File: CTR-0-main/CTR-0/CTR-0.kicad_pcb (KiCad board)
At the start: 2 copper layers, 21 x 51 mm, 35 parts, among them J1 USB_C_Receptacle_USB2.0_14P, J2 Conn_01x20, J3 Conn_01x20, J4 Conn_01x03, SW1 SW_Push, U1 RP2040, U2 NCP1117-3.3_SOT223, U3 W25Q128JVS, U4 TVS1400DRV, Y1 12MHz

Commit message: final first route
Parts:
- C10, C11, C12, C13, C14, C15, C16, C6, C7, C8, C9: moved to B.Cu
- moved C8 59.9 mm to (193.5, 103.2)
- moved C7 59.5 mm to (193.5, 100.5)
- moved C10 58.4 mm to (195.0, 97.0), turned to 0 degrees
- moved C12 57.7 mm to (192.2, 105.0)
- moved C9 57.7 mm to (192.0, 99.5), turned to -90 degrees
- moved C13 55.6 mm to (191.8, 103.2), turned to 90 degrees
- moved C11 55.2 mm to (189.2, 103.2), turned to 90 degrees
- moved C6 55.2 mm to (188.8, 98.5), turned to 90 degrees
- moved C16 52.5 mm to (190.0, 101.5), turned to 0 degrees
- moved C14 52.0 mm to (194.8, 83.7), turned to -90 degrees
- moved C15 51.8 mm to (188.0, 101.5)
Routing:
- net +1V1: track 16.2 -> 17.5 mm, vias 0 -> 2

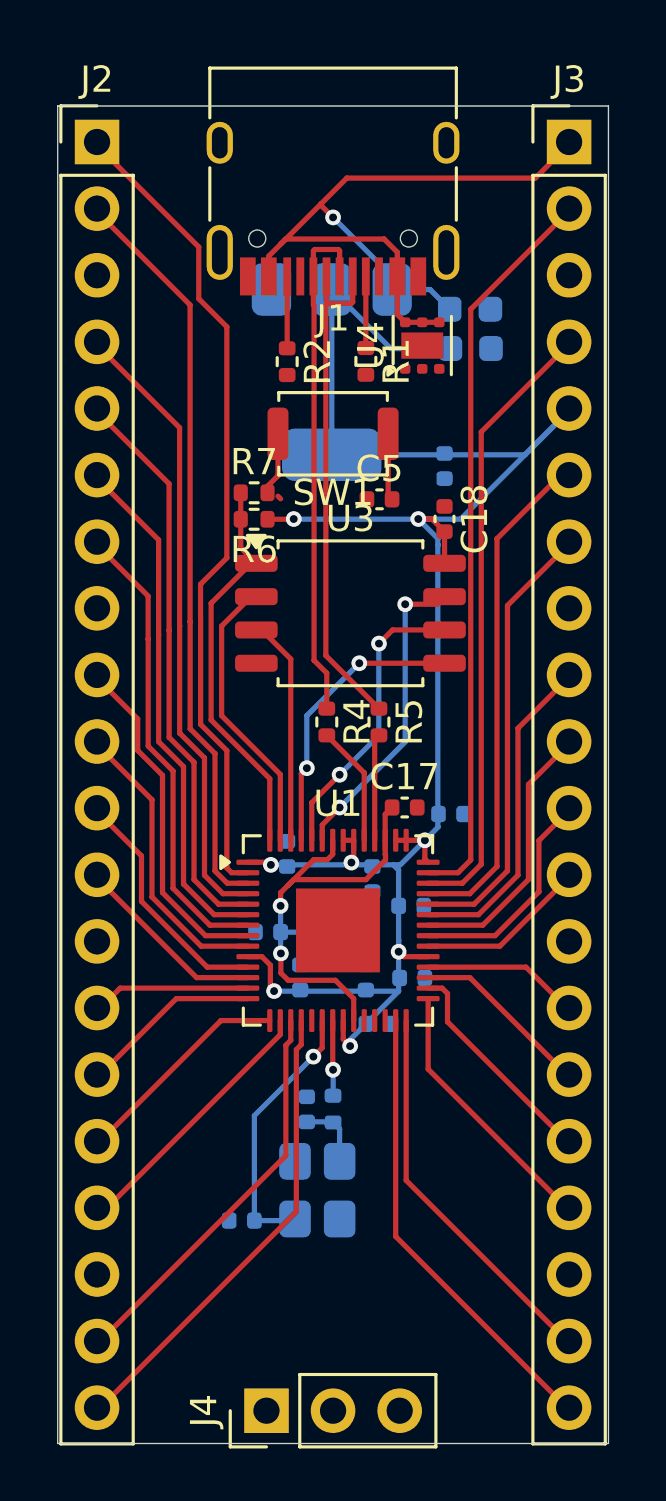
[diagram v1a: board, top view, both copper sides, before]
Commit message: reroute #2
does not fulfill drc, fix errors and clearance
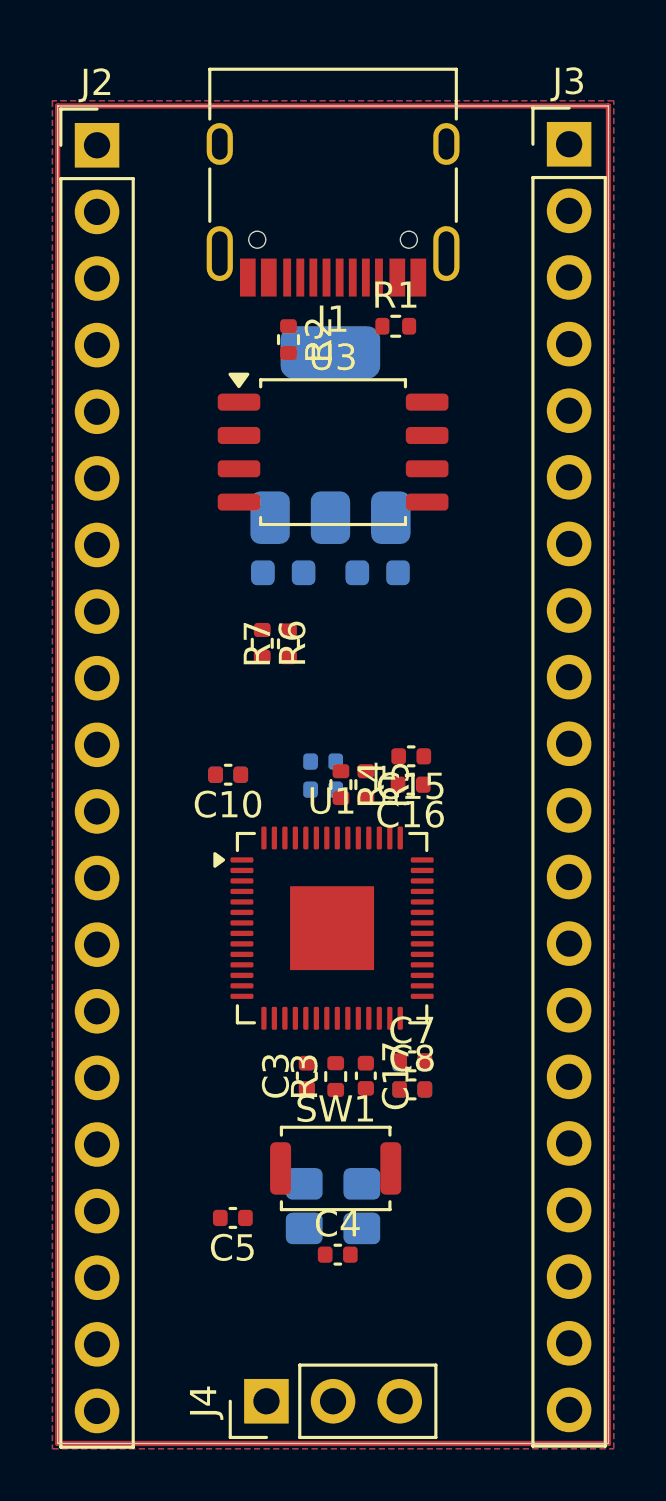
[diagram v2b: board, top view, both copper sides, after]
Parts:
- removed C13, C14: 0.1u, Capacitor_SMD:C_0402_1005Metric
- removed U4: TVS1400DRV, Package_SON:WSON-6-1EP_2x2mm_P0.65mm_EP1x1.6mm
- C10, C15, C16, C3, C4, C7, C8, R3: moved to F.Cu
- C18: moved to B.Cu
- moved SW1 28.0 mm to (190.6, 110.5), turned to 0 degrees
- moved C5 28.0 mm to (186.7, 112.4), turned to 180 degrees
- moved C18 21.8 mm to (193.5, 107.5), turned to 0 degrees
- moved C1 12.3 mm to (188.6, 87.8)
- moved C17 10.3 mm to (191.8, 107.0), turned to -90 degrees
- moved C6 9.30 mm to (193.5, 106.5), turned to 180 degrees
- moved C2 9.26 mm to (192.2, 87.8)
- moved C12 9.18 mm to (190.1, 96.1), turned to 180 degrees
- moved C15 8.64 mm to (193.5, 94.8)
- moved C10 8.63 mm to (186.5, 95.5), turned to 180 degrees
- moved C11 8.28 mm to (190.1, 95.0), turned to 180 degrees
- moved C9 6.79 mm to (186.5, 95.5), turned to 180 degrees
- moved C16 6.59 mm to (193.5, 95.9), turned to 180 degrees
- moved U3 6.18 mm to (190.5, 83.2)
- moved C3 6.05 mm to (189.5, 107.0), turned to 90 degrees
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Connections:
- net +5V renamed VBUS
- J3 pad 10: /GPIO24 -> /GPIO23
- J3 pad 11: /GPIO23 -> /RUN
- J3 pad 9: /GPIO25 -> /GPIO24
- U1 pad 37: /GPIO25 -> unconnected-(U1-GPIO25-Pad37)
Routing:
- net +3V3: track 77.8 -> 0.00 mm, vias 8 -> 0
- net /GPIO0: track 31.3 -> 0.00 mm
- net VBUS: track 29.7 -> 0.00 mm, vias 1 -> 0
- net /GPIO1: track 28.4 -> 0.00 mm
- net /GPIO29_ADC3: track 28.1 -> 0.00 mm
- net /GPIO2: track 23.9 -> 0.00 mm
- net /GPIO28_ADC2: track 23.5 -> 0.00 mm
- net /GPIO3: track 21.8 -> 0.00 mm
- net /D-: track 20.3 -> 0.00 mm
- net /GPIO4: track 19.8 -> 0.00 mm
- net /D+: track 19.7 -> 0.00 mm
- net /GPIO27_ADC1: track 19.3 -> 0.00 mm
- net /GPIO15: track 18.1 -> 0.00 mm
- net /GPIO5: track 17.7 -> 0.00 mm
- net /GPIO16: track 17.6 -> 0.00 mm
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- added copper zone on B.Cu, net GND
- added copper zone on F.Cu, net GND
